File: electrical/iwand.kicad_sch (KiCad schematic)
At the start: 12 parts, among them Q1 AO3400, Q2 AO3400, SW1 SW_Push, U1 XIAO ESP32-S3, U2 GY-33, U3 DFPlayer Mini

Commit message: Regroup wake button and DFPlayer MOSFET pins for tidiness
Swaps WAKE_BUTTON_PIN (D1->D3) and PLAYER_MOSFET_PIN (D3->D1) so the
two MOSFET gates sit on adjacent pins (D0/D1) with the button on D3,
matching the existing D4/D5 (I2C) and D8/D9 (UART) groupings. Sensor
MOSFET stays on D0. Schematic net labels updated to match (D1/D3_BTN
swapped between U1's D1 and D3 pins).

Co-Authored-By: Claude Sonnet 5 <noreply@anthropic.com>
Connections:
- net D1_BTN renamed D1
- net D1: now also R3.1; no longer SW1.1
- net D3 renamed D3_BTN
- net D3_BTN: now also SW1.1; no longer R3.1
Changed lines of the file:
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@@
     (stroke (width 0) (type solid))
   )
-  (label "D1_BTN" (at 94.76 91.27 0)
+  (label "D1" (at 94.76 91.27 0)
     (effects (font (size 1.27 1.27)) (justify left bottom))
   )
@@
     (stroke (width 0) (type solid))
   )
-  (label "D1_BTN" (at 99.84 140.0 0)
+  (label "D3_BTN" (at 99.84 140.0 0)
     (effects (font (size 1.27 1.27)) (justify left bottom))
   )
@@
     (stroke (width 0) (type solid))
   )
-  (label "D3" (at 125.24 84.92 0)
+  (label "D3_BTN" (at 125.24 84.92 0)
     (effects (font (size 1.27 1.27)) (justify left bottom))
   )
@@
     (stroke (width 0) (type solid))
   )
-  (label "D3" (at 150.0 96.11 0)
+  (label "D1" (at 150.0 96.11 0)
     (effects (font (size 1.27 1.27)) (justify left bottom))
   )

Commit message: Add sensor calibration, switch GY-33 to UART, fix wake loop
- Calibration mode: hold SW1 at cold power-up, then press SW1 on a white
  and a black target. The white and black points are saved to NVS; the
  module's own white balance is also run and saved to its flash.
- Classify colours in firmware from raw RGB: normalise to the calibrated
  black/white points, gamma-encode to match perceived brightness, then
  pick Black/White/Gray or a hue band. The library's colour() misreads
  the GY-33's colour byte (bit flags, not an index).
- Drive the GY-33 over UART (its factory default) on D8/D9; it never
  answered over I2C.
- Swap buses between D4/D5 (now DFPlayer UART) and D8/D9 (now GY-33),
  in both firmware and schematic.
- Fix a wake loop: enable the RTC pull-up on SW1 before deep sleep, and
  wait for SW1 release so a held button doesn't re-trigger.
- Debug aids: boot reset/wake reason, sensor read details, and a wait
  for the USB serial monitor at boot (SERIAL_WAIT_MS).

Co-Authored-By: Claude Opus 5.5 <noreply@anthropic.com>
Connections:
- net SCL: now also U1.9 (D9_SCL); no longer U1.7 (SCL)
- net SDA: now also U1.8 (D8_SDA); no longer U1.6 (SDA)
- net UART_RX: now also U1.6 (D4_RX); no longer U1.8 (D8_RX)
- net UART_TX: now also U1.7 (D5_TX); no longer U1.9 (D9_TX)
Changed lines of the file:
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@@
     (stroke (width 0) (type solid))
   )
-  (label "SDA" (at 125.24 87.46 0)
+  (label "UART_RX" (at 125.24 87.46 0)
     (effects (font (size 1.27 1.27)) (justify left bottom))
   )
@@
     (stroke (width 0) (type solid))
   )
-  (label "SCL" (at 125.24 90.0 0)
+  (label "UART_TX" (at 125.24 90.0 0)
     (effects (font (size 1.27 1.27)) (justify left bottom))
   )
@@
     (stroke (width 0) (type solid))
   )
-  (label "UART_TX" (at 125.24 95.08 0)
+  (label "SCL" (at 125.24 95.08 0)
     (effects (font (size 1.27 1.27)) (justify left bottom))
   )
@@
     (stroke (width 0) (type solid))
   )
-  (label "UART_RX" (at 125.24 92.54 0)
+  (label "SDA" (at 125.24 92.54 0)
     (effects (font (size 1.27 1.27)) (justify left bottom))
   )

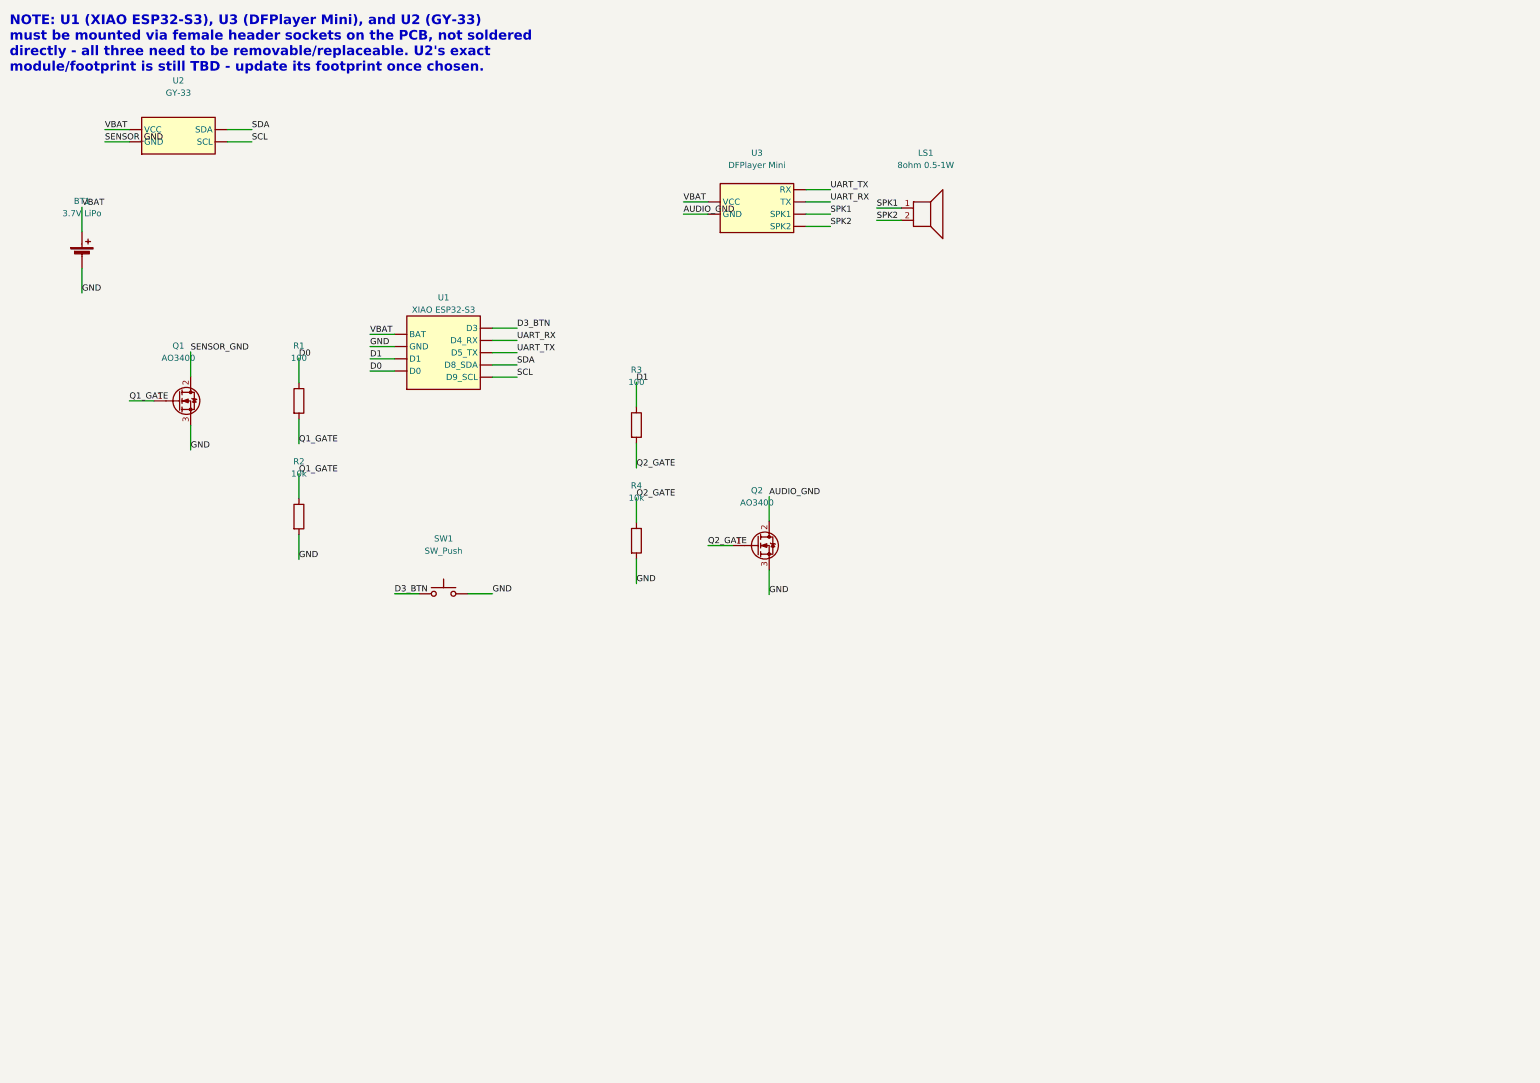
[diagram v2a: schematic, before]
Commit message: Add PCB footprints and connector-based schematic for board layout
- New project footprint library electrical/iwand.pretty (via fp-lib-table):
  XIAO ESP32S3 and DFPlayer Mini on female header sockets, and the AO3400
  on its SOT-23 adapter board with pads in the adapter's S-D-G order.
- Module symbols now have all header pins (XIAO 14, DFPlayer 16), with
  unused pins marked no-connect.
- Off-board parts become JST-PH side-entry connectors: J1 GY-33
  (GND/DR/CT/VCC), J2 speaker, J3 wake button SW1, J4 LiPo. J5 takes
  wires to the XIAO's underside battery pads.
- Through-hole resistors; footprints assigned to every part. GY-33 nets
  renamed GY33_DR/GY33_CT to match its UART use.
- Update electrical, mechanical, firmware and root docs to match.
- Ignore reference/ and KiCad lock/history files.

Co-Authored-By: Claude Opus 5.5 <noreply@anthropic.com>
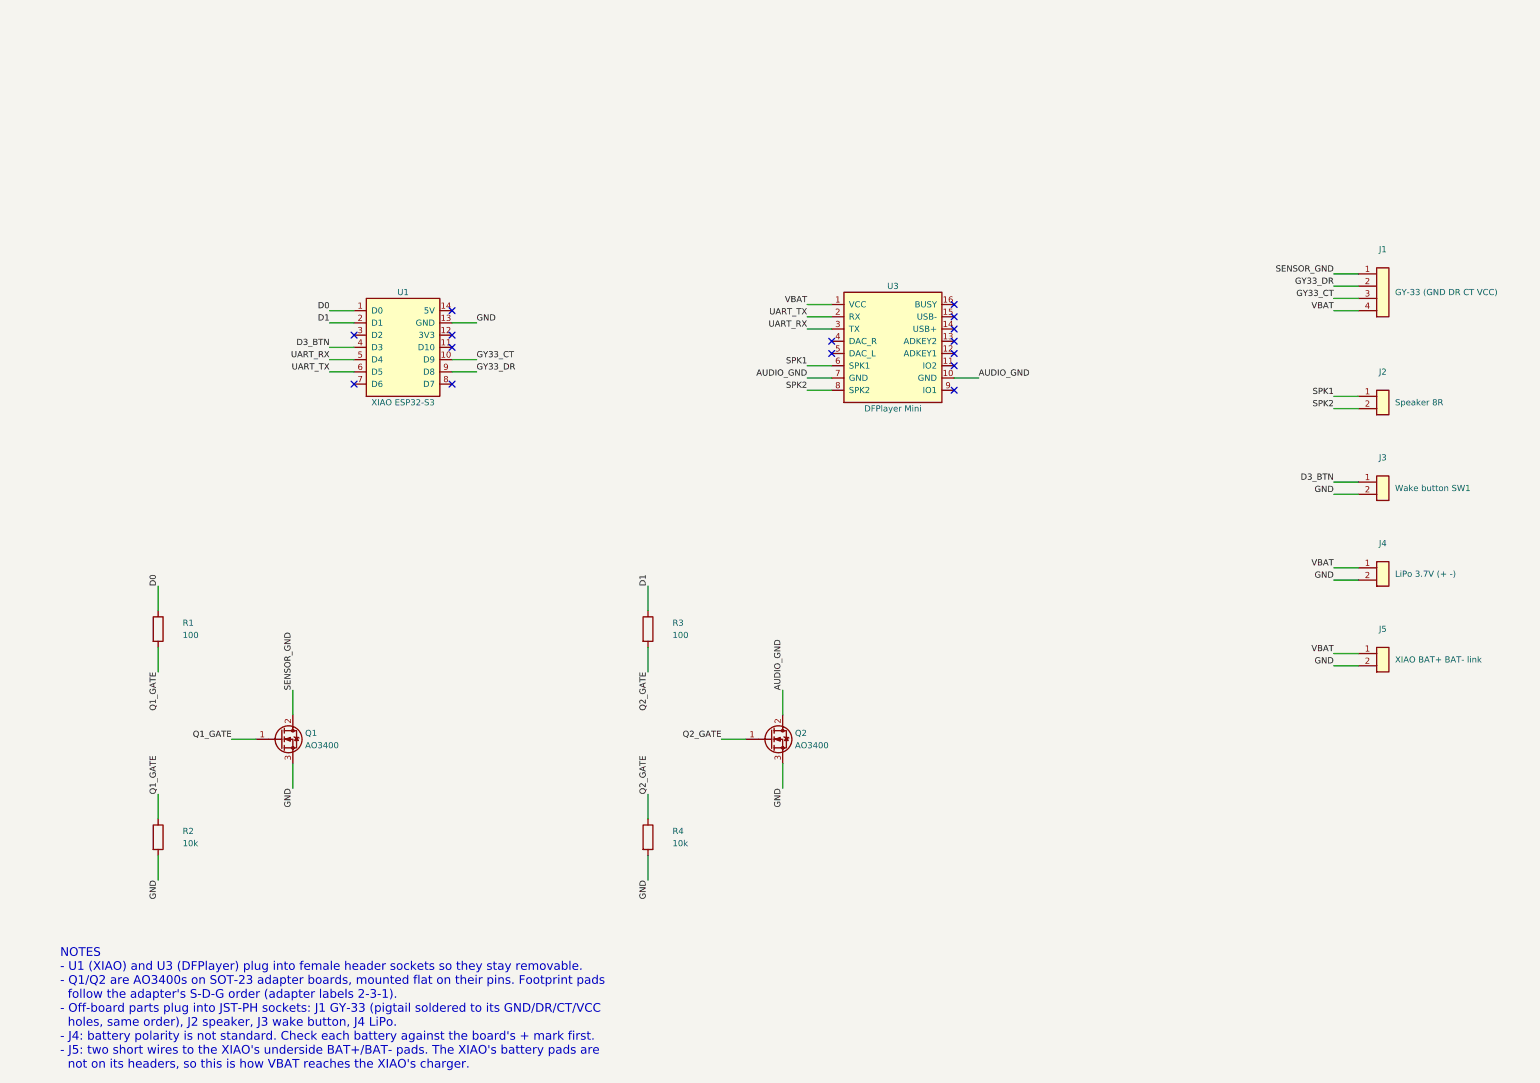
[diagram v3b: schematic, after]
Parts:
- removed BT1: 3.7V LiPo, symbol Device:Battery_Cell
- removed LS1: 8ohm 0.5-1W, symbol Device:Speaker
- removed SW1: SW_Push, symbol Switch:SW_Push
- removed U2: GY-33, symbol wand_parts:GY33_Breakout
- added J1: GY-33 (GND DR CT VCC), Connector_JST:JST_PH_S4B-PH-K_1x04_P2.00mm_Horizontal, symbol Connector_Generic:Conn_01x04
- added J2: Speaker 8R, Connector_JST:JST_PH_S2B-PH-K_1x02_P2.00mm_Horizontal, symbol Connector_Generic:Conn_01x02
- added J3: Wake button SW1, Connector_JST:JST_PH_S2B-PH-K_1x02_P2.00mm_Horizontal, symbol Connector_Generic:Conn_01x02
- added J4: LiPo 3.7V (+ -), Connector_JST:JST_PH_S2B-PH-K_1x02_P2.00mm_Horizontal, symbol Connector_Generic:Conn_01x02
- added J5: XIAO BAT+ BAT- link, Connector_PinHeader_2.54mm:PinHeader_1x02_P2.54mm_Vertical, symbol Connector_Generic:Conn_01x02
- Q1, Q2: footprint (none) -> iwand:AO3400_SOT23_Adapter
- R1, R2, R3, R4: footprint (none) -> Resistor_THT:R_Axial_DIN0207_L6.3mm_D2.5mm_P2.54mm_Vertical
- U1: footprint (none) -> iwand:XIAO_ESP32S3_Socket
- U3: footprint (none) -> iwand:DFPlayer_Mini_Socket
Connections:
- net AUDIO_GND: now also U3.10 (GND), U3.7 (GND); no longer U3.2 (GND)
- net D0: now also U1.1 (D0); no longer U1.4 (D0)
- net D1: now also U1.2 (D1); no longer U1.3 (D1)
- net D3_BTN: now also U1.4 (D3), J3.1 (Pin_1); no longer U1.5 (D3)
- net GND: now also U1.13 (GND), J3.2 (Pin_2), J4.2 (Pin_2), J5.2 (Pin_2); no longer U1.2 (GND)
- net SENSOR_GND: now also J1.1 (Pin_1)
- net SPK1: now also U3.6 (SPK1), J2.1 (Pin_1); no longer U3.5 (SPK1)
- net SPK2: now also U3.8 (SPK2), J2.2 (Pin_2); no longer U3.6 (SPK2)
- net UART_RX: now also U1.5 (D4), U3.3 (TX); no longer U1.6 (D4_RX), U3.4 (TX)
- net UART_TX: now also U1.6 (D5), U3.2 (RX); no longer U1.7 (D5_TX), U3.3 (RX)
- net VBAT: now also J1.4 (Pin_4), J4.1 (Pin_1), J5.1 (Pin_1); no longer U1.1 (BAT)
- net SCL renamed GY33_DR
- net GY33_DR: now also J1.2 (Pin_2)
- net SDA: no longer names the net of U1.8 (D7)
- new net GY33_CT: J1.3 (Pin_3), U1.10 (D9)
- no-connect marks 0 -> 15
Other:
- note added: "NOTES - U1 (XIAO) and U3 (DFPlayer) plug into female header sockets so they stay removable. - Q1/Q2 are AO3400s on SOT-23 adapter boards, mounted flat on their pins. Footprint pads follow the adapter's S-D-G order (adapter labels 2-3-1). - Off-board parts plug into JST-PH sockets: J1 GY-33 (pigtail soldered to its GND/DR/CT/VCC holes, same order), J2 speaker, J3 wake button, J4 LiPo. - J4: batter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"
- note removed: "NOTE: U1 (XIAO ESP32-S3), U3 (DFPlayer Mini), and U2 (GY-33) must be mounted via female header sockets on the PCB, not soldered directly - all three need to be removable/replaceable. U2's exact module/footprint is still TBD - update its footprint once chosen."
- moved on the sheet: Q1, Q2, R1, R2, R3, R4
